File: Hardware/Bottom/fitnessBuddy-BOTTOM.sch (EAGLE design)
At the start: 38 parts, among them U4 PCF8523

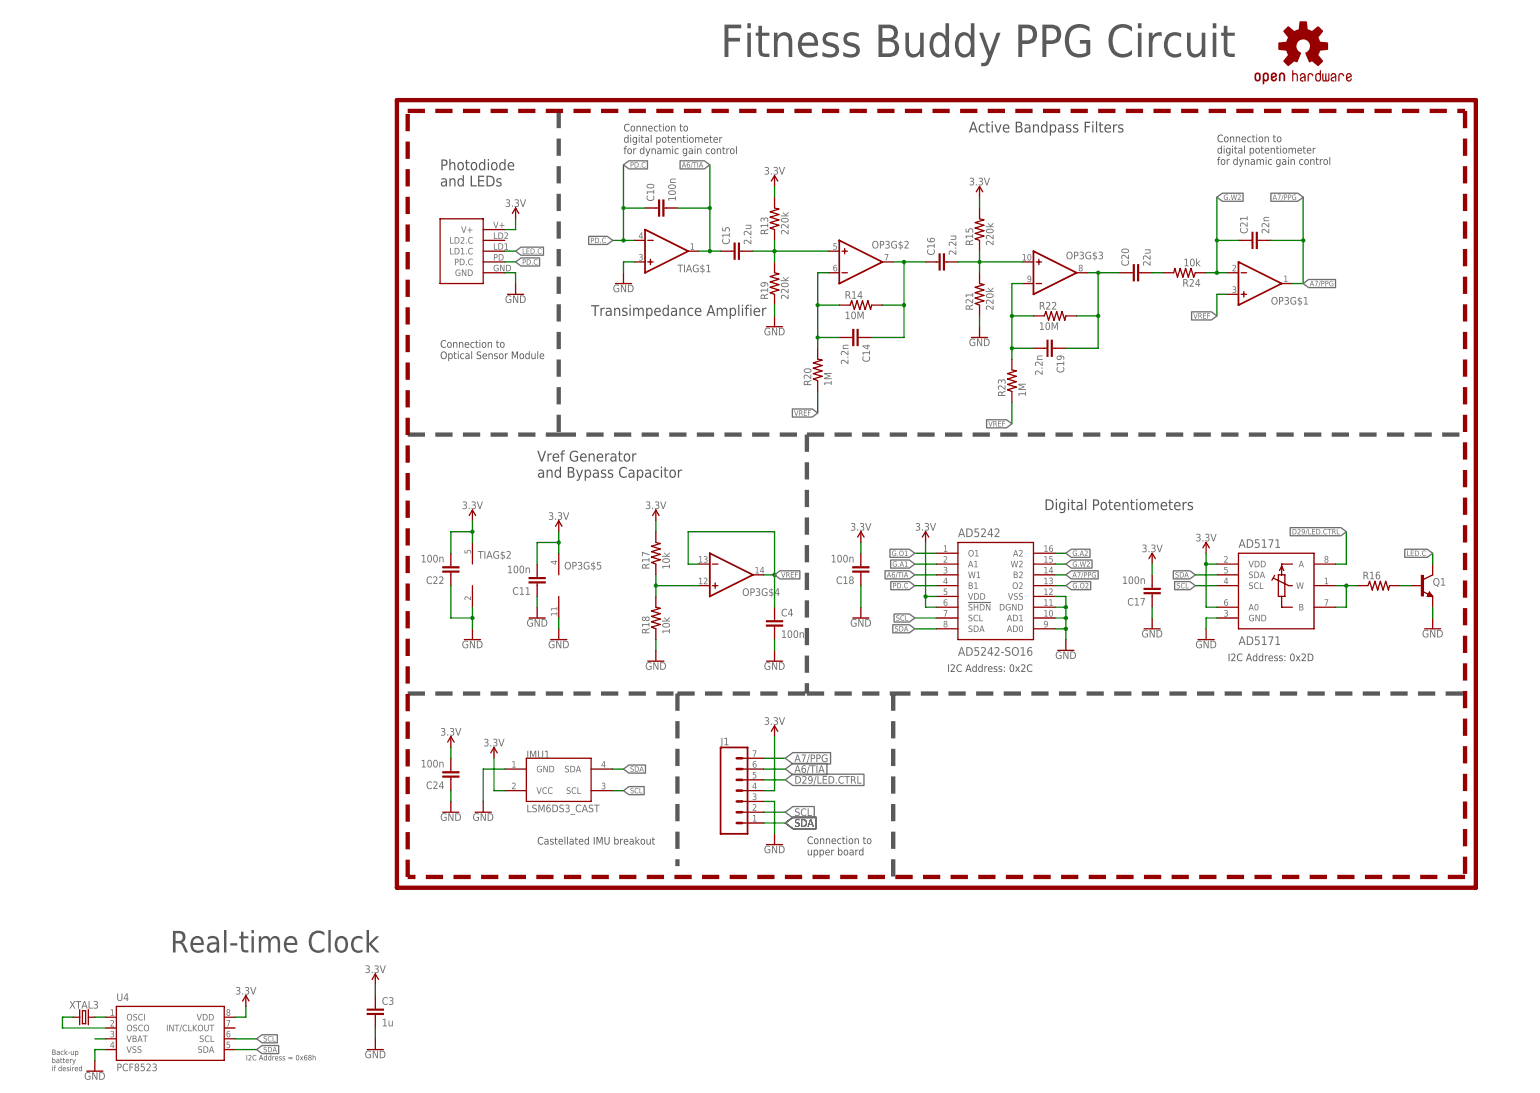
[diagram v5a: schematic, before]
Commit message: reorganized bottom boards, added RTC to bottom board, and added notes to top schematic
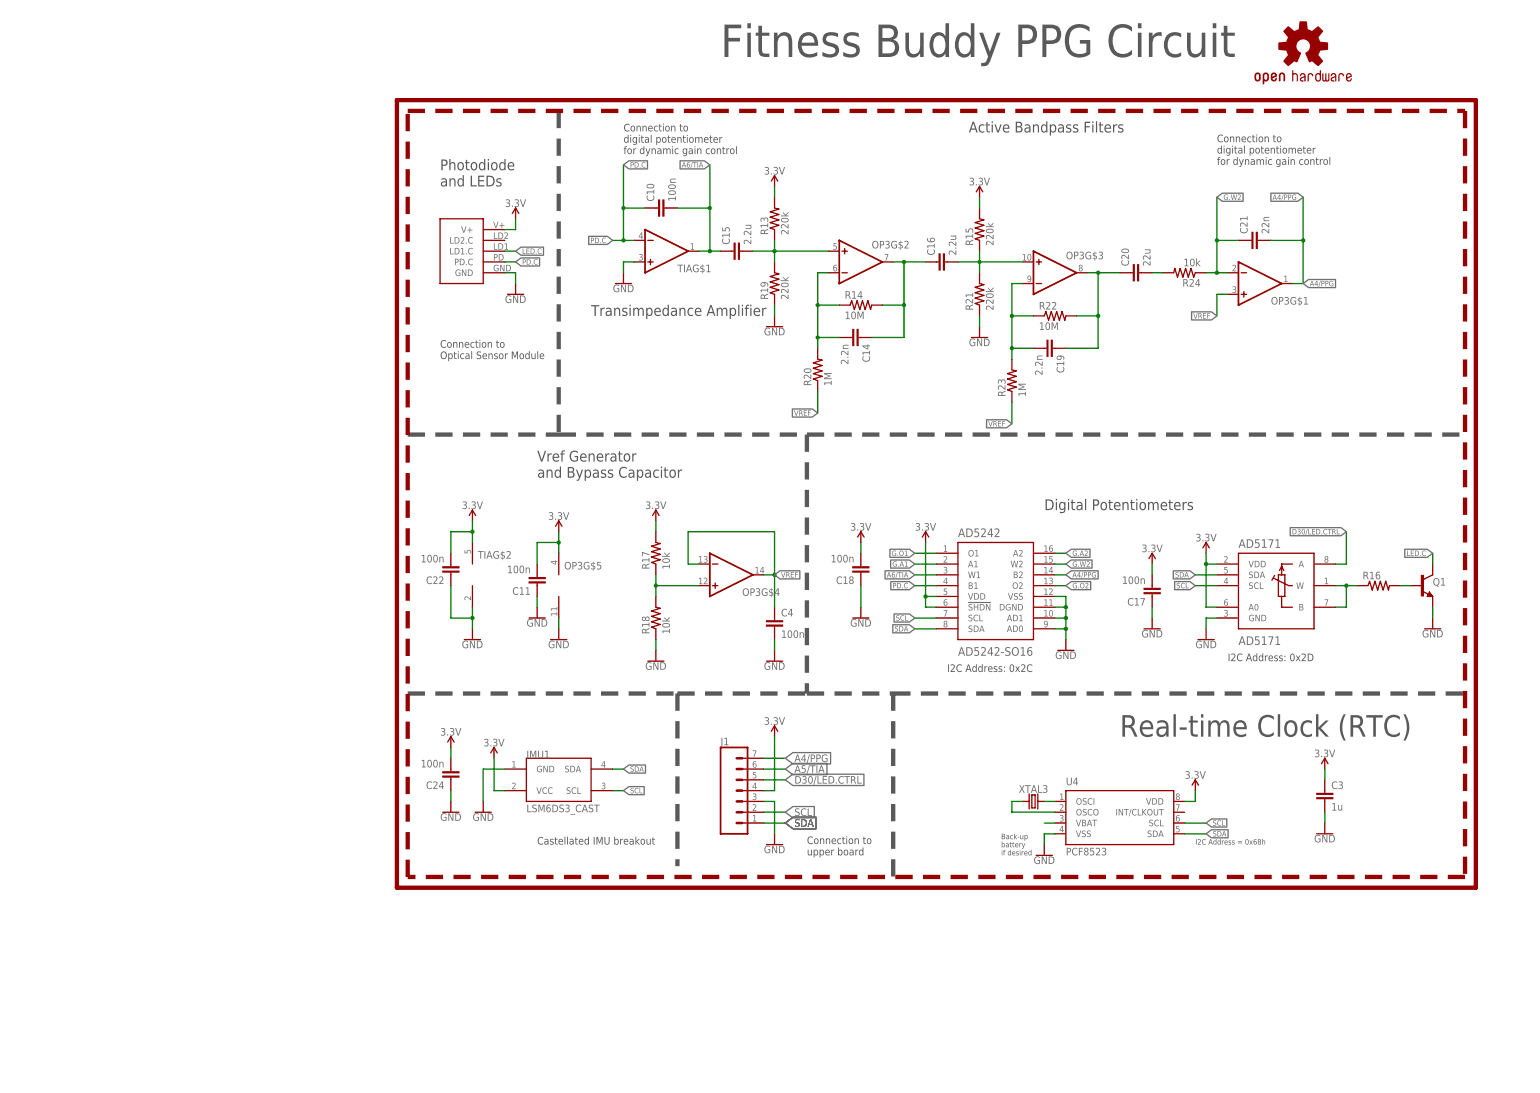
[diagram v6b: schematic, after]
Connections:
- net A7/PPG renamed A4/PPG
- net D29/LED.CTRL renamed D30/LED.CTRL
- new net A5/TIA: J1.6
- net A6/TIA: no longer J1.6
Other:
- note added: "Real-time Clock (RTC)"
- note removed: "Real-time Clock"
- moved on the sheet: C3, U4, XTAL3
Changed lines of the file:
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@@
 <text x="101.6" y="27.94" size="1.778" layer="97" ratio="15">I2C Address: 0x2C</text>
 <text x="167.64" y="30.48" size="1.778" layer="97" ratio="15">I2C Address: 0x2D</text>
-<text x="-63.5" y="-63.5" size="1.27" layer="97">I2C Address = 0x68h</text>
-<text x="-109.22" y="-66.04" size="1.27" layer="97">Back-up
+<text x="160.02" y="-12.7" size="1.27" layer="97">I2C Address = 0x68h</text>
+<text x="114.3" y="-15.24" size="1.27" layer="97">Back-up
 battery
 if desired</text>
-<text x="-81.28" y="-38.1" size="5.08" layer="97" font="vector" ratio="15">Real-time Clock</text>
+<text x="142.24" y="12.7" size="5.08" layer="97" font="vector" ratio="15">Real-time Clock (RTC)</text>
 <wire x1="-25.4" y1="-20.32" x2="-25.4" y2="160.02" width="1.016" layer="94" style="longdash"/>
 <wire x1="-25.4" y1="160.02" x2="223.52" y2="160.02" width="1.016" layer="94" style="longdash"/>
@@
 <attribute name="NAME" x="48.26" y="10.668" size="1.778" layer="95" font="vector"/>
 </instance>
-<instance part="GND1" gate="G$1" x="-99.06" y="-66.04" smashed="yes">
-<attribute name="VALUE" x="-99.06" y="-66.294" size="1.778" layer="96" align="top-center"/>
-</instance>
-<instance part="GND5" gate="G$1" x="-33.02" y="-60.96" smashed="yes">
-<attribute name="VALUE" x="-33.02" y="-61.214" size="1.778" layer="96" align="top-center"/>
-</instance>
-<instance part="SUPPLY10" gate="G$1" x="-63.5" y="-50.8" smashed="yes">
-<attribute name="VALUE" x="-63.5" y="-48.006" size="1.778" layer="96" align="bottom-center"/>
-</instance>
-<instance part="C3" gate="G$1" x="-33.02" y="-53.34" smashed="yes">
-<attribute name="NAME" x="-31.496" y="-50.419" size="1.778" layer="95"/>
-<attribute name="VALUE" x="-31.496" y="-55.499" size="1.778" layer="96"/>
-</instance>
-<instance part="SUPPLY11" gate="G$1" x="-33.02" y="-45.72" smashed="yes">
-<attribute name="VALUE" x="-33.02" y="-42.926" size="1.778" layer="96" align="bottom-center"/>
-</instance>
-<instance part="XTAL3" gate="G$1" x="-101.6" y="-53.34" smashed="yes">
-<attribute name="NAME" x="-101.6" y="-51.308" size="1.778" layer="95" font="vector" align="bottom-center"/>
-</instance>
-<instance part="U4" gate="G$1" x="-81.28" y="-55.88" smashed="yes">
-<attribute name="NAME" x="-93.98" y="-49.53" size="1.778" layer="95"/>
-<attribute name="VALUE" x="-93.98" y="-66.04" size="1.778" layer="96"/>
-<attribute name="DIGIKEY" x="-81.28" y="-55.88" size="1.27" layer="96" display="off"/>
-<attribute name="I2C_ADDRESS" x="-81.28" y="-55.88" size="1.27" layer="96" display="off"/>
-<attribute name="MFN" x="-81.28" y="-55.88" size="1.27" layer="96" display="off"/>
-<attribute name="MFN_MANUFACTURER" x="-81.28" y="-55.88" size="1.27" layer="96" display="off"/>
+<instance part="GND1" gate="G$1" x="124.46" y="-15.24" smashed="yes">
+<attribute name="VALUE" x="124.46" y="-15.494" size="1.778" layer="96" align="top-center"/>
+</instance>
+<instance part="GND5" gate="G$1" x="190.5" y="-10.16" smashed="yes">
+<attribute name="VALUE" x="190.5" y="-10.414" size="1.778" layer="96" align="top-center"/>
+</instance>
+<instance part="SUPPLY10" gate="G$1" x="160.02" y="0" smashed="yes">
+<attribute name="VALUE" x="160.02" y="2.794" size="1.778" layer="96" align="bottom-center"/>
+</instance>
+<instance part="C3" gate="G$1" x="190.5" y="-2.54" smashed="yes">
+<attribute name="NAME" x="192.024" y="0.381" size="1.778" layer="95"/>
+<attribute name="VALUE" x="192.024" y="-4.699" size="1.778" layer="96"/>
+</instance>
+<instance part="SUPPLY11" gate="G$1" x="190.5" y="5.08" smashed="yes">
+<attribute name="VALUE" x="190.5" y="7.874" size="1.778" layer="96" align="bottom-center"/>
+</instance>
+<instance part="XTAL3" gate="G$1" x="121.92" y="-2.54" smashed="yes">
+<attribute name="NAME" x="121.92" y="-0.508" size="1.778" layer="95" font="vector" align="bottom-center"/>
+</instance>
+<instance part="U4" gate="G$1" x="142.24" y="-5.08" smashed="yes">
+<attribute name="NAME" x="129.54" y="1.27" size="1.778" layer="95"/>
+<attribute name="VALUE" x="129.54" y="-15.24" size="1.778" layer="96"/>
+<attribute name="DIGIKEY" x="142.24" y="-5.08" size="1.27" layer="96" display="off"/>
+<attribute name="I2C_ADDRESS" x="142.24" y="-5.08" size="1.27" layer="96" display="off"/>
+<attribute name="MFN" x="142.24" y="-5.08" size="1.27" layer="96" display="off"/>
+<attribute name="MFN_MANUFACTURER" x="142.24" y="-5.08" size="1.27" layer="96" display="off"/>
 </instance>
 <instance part="GND2" gate="G$1" x="60.96" y="-12.7" smashed="yes">
@@
 </segment>
 <segment>
-<wire x1="-96.52" y1="-60.96" x2="-99.06" y2="-60.96" width="0.1524" layer="91"/>
-<wire x1="-99.06" y1="-63.5" x2="-99.06" y2="-60.96" width="0.1524" layer="91"/>
+<wire x1="127" y1="-10.16" x2="124.46" y2="-10.16" width="0.1524" layer="91"/>
+<wire x1="124.46" y1="-12.7" x2="124.46" y2="-10.16" width="0.1524" layer="91"/>
 <pinref part="GND1" gate="G$1" pin="GND"/>
 <pinref part="U4" gate="G$1" pin="VSS"/>
 </segment>
 <segment>
-<wire x1="-33.02" y1="-58.42" x2="-33.02" y2="-55.88" width="0.1524" layer="91"/>
+<wire x1="190.5" y1="-7.62" x2="190.5" y2="-5.08" width="0.1524" layer="91"/>
 <pinref part="GND5" gate="G$1" pin="GND"/>
 <pinref part="C3" gate="G$1" pin="2"/>
@@
 </segment>
 <segment>
-<wire x1="-66.04" y1="-53.34" x2="-63.5" y2="-53.34" width="0.1524" layer="91"/>
-<wire x1="-63.5" y1="-50.8" x2="-63.5" y2="-53.34" width="0.1524" layer="91"/>
+<wire x1="157.48" y1="-2.54" x2="160.02" y2="-2.54" width="0.1524" layer="91"/>
+<wire x1="160.02" y1="0" x2="160.02" y2="-2.54" width="0.1524" layer="91"/>
 <pinref part="SUPPLY10" gate="G$1" pin="3.3V"/>
 <pinref part="U4" gate="G$1" pin="VDD"/>
@@
 <pinref part="C3" gate="G$1" pin="1"/>
 <pinref part="SUPPLY11" gate="G$1" pin="3.3V"/>
-<wire x1="-33.02" y1="-45.72" x2="-33.02" y2="-48.26" width="0.1524" layer="91"/>
+<wire x1="190.5" y1="5.08" x2="190.5" y2="2.54" width="0.1524" layer="91"/>
 </segment>
 <segment>
@@
 </segment>
 <segment>
-<wire x1="-66.04" y1="-60.96" x2="-60.96" y2="-60.96" width="0.1524" layer="91"/>
-<label x="-60.96" y="-60.96" size="1.27" layer="95" xref="yes"/>
+<wire x1="157.48" y1="-10.16" x2="162.56" y2="-10.16" width="0.1524" layer="91"/>
+<label x="162.56" y="-10.16" size="1.27" layer="95" xref="yes"/>
 <pinref part="U4" gate="G$1" pin="SDA"/>
 </segment>
@@
 </segment>
 <segment>
-<label x="-60.96" y="-58.42" size="1.27" layer="95" xref="yes"/>
-<wire x1="-66.04" y1="-58.42" x2="-60.96" y2="-58.42" width="0.1524" layer="91"/>
+<label x="162.56" y="-7.62" size="1.27" layer="95" xref="yes"/>
+<wire x1="157.48" y1="-7.62" x2="162.56" y2="-7.62" width="0.1524" layer="91"/>
 <pinref part="U4" gate="G$1" pin="SCL"/>
 </segment>
@@
 <junction x="45.72" y="127"/>
 </segment>
-<segment>
-<pinref part="J1" gate="G$1" pin="6"/>
-<wire x1="58.42" y1="5.08" x2="63.5" y2="5.08" width="0.1524" layer="91"/>
-<label x="63.5" y="5.08" size="1.778" layer="95" xref="yes"/>
-</segment>
 </net>
 <net name="PD.C" class="0">
@@
 </segment>
 </net>
-<net name="D29/LED.CTRL" class="0">
+<net name="D30/LED.CTRL" class="0">
 <segment>
 <pinref part="AD5171" gate="G$1" pin="A"/>
@@
 </segment>
 </net>
-<net name="A7/PPG" class="0">
+<net name="A4/PPG" class="0">
 <segment>
 <wire x1="127" y1="50.8" x2="129.54" y2="50.8" width="0.1524" layer="91"/>
@@
 <net name="N$5" class="0">
 <segment>
-<wire x1="-96.52" y1="-55.88" x2="-106.68" y2="-55.88" width="0.1524" layer="91"/>
-<wire x1="-106.68" y1="-55.88" x2="-106.68" y2="-53.34" width="0.1524" layer="91"/>
-<wire x1="-106.68" y1="-53.34" x2="-104.14" y2="-53.34" width="0.1524" layer="91"/>
+<wire x1="127" y1="-5.08" x2="116.84" y2="-5.08" width="0.1524" layer="91"/>
+<wire x1="116.84" y1="-5.08" x2="116.84" y2="-2.54" width="0.1524" layer="91"/>
+<wire x1="116.84" y1="-2.54" x2="119.38" y2="-2.54" width="0.1524" layer="91"/>
 <pinref part="XTAL3" gate="G$1" pin="1"/>
 <pinref part="U4" gate="G$1" pin="OSCO"/>
@@
 <net name="N$6" class="0">
 <segment>
-<wire x1="-99.06" y1="-53.34" x2="-96.52" y2="-53.34" width="0.1524" layer="91"/>
+<wire x1="124.46" y1="-2.54" x2="127" y2="-2.54" width="0.1524" layer="91"/>
 <pinref part="XTAL3" gate="G$1" pin="2"/>
 <pinref part="U4" gate="G$1" pin="OSCI"/>
@@
 <net name="VBATT" class="0">
 <segment>
-<wire x1="-96.52" y1="-58.42" x2="-99.06" y2="-58.42" width="0.1524" layer="91"/>
+<wire x1="127" y1="-7.62" x2="124.46" y2="-7.62" width="0.1524" layer="91"/>
 <pinref part="U4" gate="G$1" pin="VBAT"/>
 </segment>
 </net>
+<net name="A5/TIA" class="0">
+<segment>
+<pinref part="J1" gate="G$1" pin="6"/>
+<wire x1="58.42" y1="5.08" x2="63.5" y2="5.08" width="0.1524" layer="91"/>
+<label x="63.5" y="5.08" size="1.778" layer="95" xref="yes"/>
+</segment>
+</net>

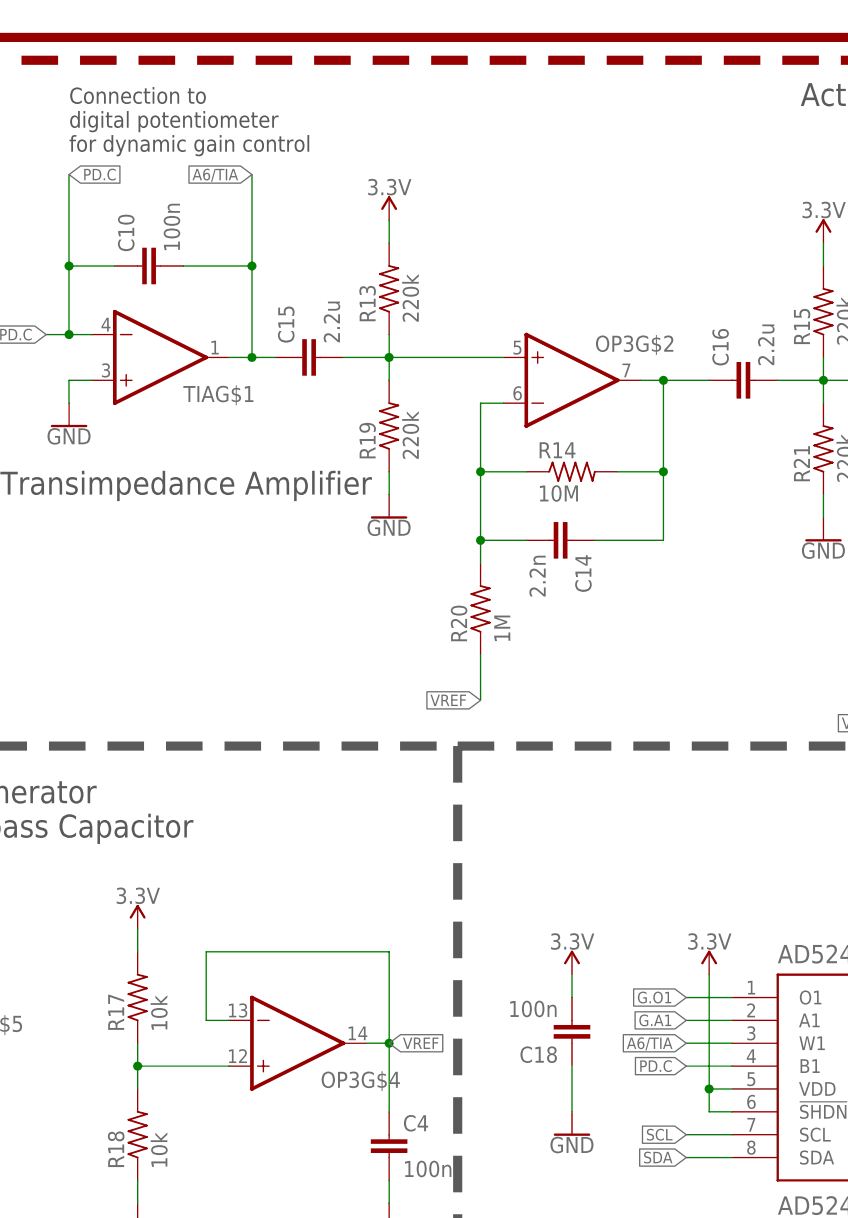
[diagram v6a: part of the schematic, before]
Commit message: fixed pinout connecting bottom and top boards also added ppg module files
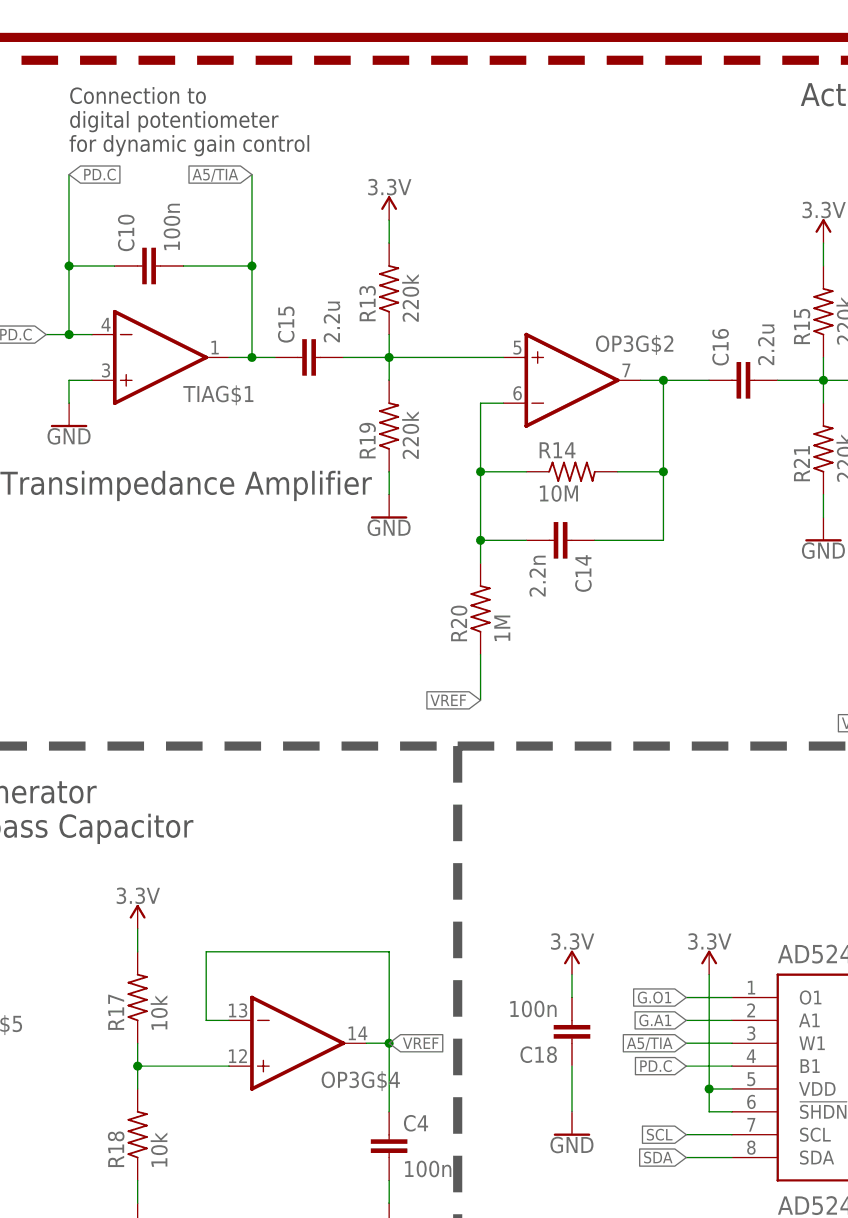
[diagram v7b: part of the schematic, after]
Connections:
- removed net A6/TIA: AD5242.W1, C10.2, C15.1, TIAG$1.OUT
- net A5/TIA: now also AD5242.W1, C10.2, C15.1, TIAG$1.OUT
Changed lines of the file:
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@@
 <?xml version="1.0" encoding="utf-8"?>
 <!DOCTYPE eagle SYSTEM "eagle.dtd">
-<eagle version="9.6.1">
+<eagle version="9.6.2">
 <drawing>
 <settings>
@@
 </segment>
 </net>
-<net name="A6/TIA" class="0">
-<segment>
-<wire x1="99.06" y1="50.8" x2="93.98" y2="50.8" width="0.1524" layer="91"/>
-<label x="93.98" y="50.8" size="1.27" layer="95" rot="R180" xref="yes"/>
-<pinref part="AD5242" gate="G$1" pin="W1"/>
-</segment>
-<segment>
-<pinref part="C10" gate="G$1" pin="2"/>
-<wire x1="38.1" y1="137.16" x2="45.72" y2="137.16" width="0.1524" layer="91"/>
-<wire x1="45.72" y1="137.16" x2="45.72" y2="127" width="0.1524" layer="91"/>
-<wire x1="45.72" y1="137.16" x2="45.72" y2="147.32" width="0.1524" layer="91"/>
-<junction x="45.72" y="137.16"/>
-<label x="45.72" y="147.32" size="1.27" layer="95" rot="R180" xref="yes"/>
-<pinref part="C15" gate="G$1" pin="1"/>
-<wire x1="48.26" y1="127" x2="45.72" y2="127" width="0.1524" layer="91"/>
-<pinref part="TIA" gate="G$1" pin="OUT"/>
-<wire x1="43.18" y1="127" x2="45.72" y2="127" width="0.1524" layer="91"/>
-<junction x="45.72" y="127"/>
-</segment>
-</net>
 <net name="PD.C" class="0">
 <segment>
@@
 <label x="63.5" y="5.08" size="1.778" layer="95" xref="yes"/>
 </segment>
-</net>
+<segment>
+<wire x1="99.06" y1="50.8" x2="93.98" y2="50.8" width="0.1524" layer="91"/>
+<label x="93.98" y="50.8" size="1.27" layer="95" rot="R180" xref="yes"/>
+<pinref part="AD5242" gate="G$1" pin="W1"/>
+</segment>
+<segment>
+<pinref part="C10" gate="G$1" pin="2"/>
+<wire x1="38.1" y1="137.16" x2="45.72" y2="137.16" width="0.1524" layer="91"/>
+<wire x1="45.72" y1="137.16" x2="45.72" y2="127" width="0.1524" layer="91"/>
+<wire x1="45.72" y1="137.16" x2="45.72" y2="147.32" width="0.1524" layer="91"/>
+<junction x="45.72" y="137.16"/>
+<label x="45.72" y="147.32" size="1.27" layer="95" rot="R180" xref="yes"/>
+<pinref part="C15" gate="G$1" pin="1"/>
+<wire x1="48.26" y1="127" x2="45.72" y2="127" width="0.1524" layer="91"/>
+<pinref part="TIA" gate="G$1" pin="OUT"/>
+<wire x1="43.18" y1="127" x2="45.72" y2="127" width="0.1524" layer="91"/>
+<junction x="45.72" y="127"/>
+</segment>
+</net>
